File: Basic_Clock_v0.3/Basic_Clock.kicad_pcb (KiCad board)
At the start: 2 copper layers, 97.8 x 71.1 mm, 30 parts, among them J1 Conn_01x04_Female, J2 Conn_01x04_Female, J4 Screw_Terminal_01x02, SW1 SW_Push_Reset, SW2 SW_Push, SW3 SW_Push, SW4 SW_Push, U1 LM317_TO-220, U2 ATmega328P-PU, Y1 16Mhz 16Mhz

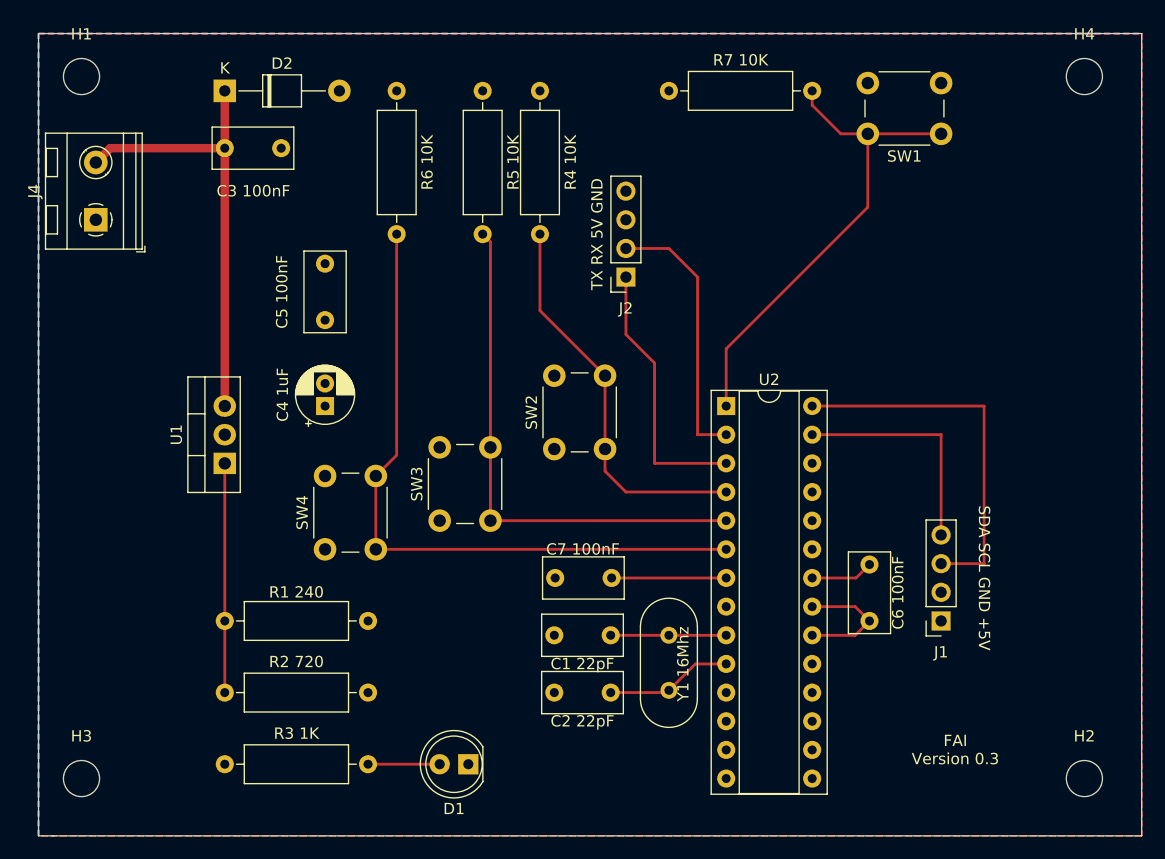
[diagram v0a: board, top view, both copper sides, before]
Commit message: New Testprogram Reorganized Folder
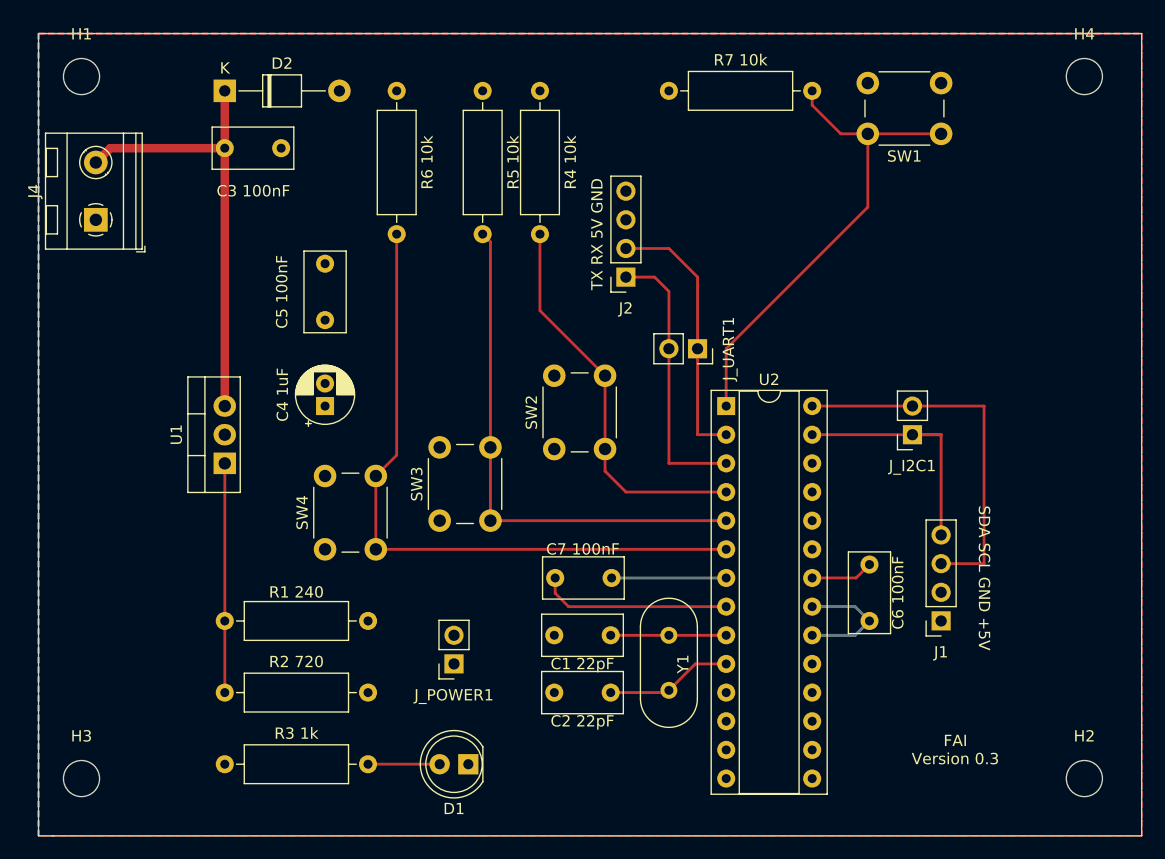
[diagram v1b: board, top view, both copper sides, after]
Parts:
- added J_I2C1: Conn_01x02_Female, Connector THT:PinSocket_1x02_P2.54mm_Vertical, F.Cu at (114.3, 139.7)
- added J_POWER1: Conn_01x02_Female, Connector THT:PinSocket_1x02_P2.54mm_Vertical, F.Cu at (73.7, 160.0)
- added J_UART1: Conn_01x02_Female, Connector THT:PinSocket_1x02_P2.54mm_Vertical, F.Cu at (95.2, 132.1)
- R3 1k: renamed from R3 1K
- R4 10k: renamed from R4 10K
- R5 10k: renamed from R5 10K
- R6 10k: renamed from R6 10K
- R7 10k: renamed from R7 10K
- Y1: renamed from Y1 16Mhz
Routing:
- net GND: track 5.57 -> 22.6 mm
- net /SDA: track 20.3 -> 22.9 mm
- net /TX: track 23.9 -> 24.7 mm
- net +5V: vias 2 -> 0
